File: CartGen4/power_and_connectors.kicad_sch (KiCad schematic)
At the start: 35 parts, among them U1 TPS65266-1RHBR

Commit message: Updated field information
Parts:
- A1: Notes (none) -> Edge connector and board outline of the cartridge
- C1, C10, C12, C13, C15, C16, C5, C6, C7, C8: Package ID (none) -> 0603
- C11, C2, C4, C9: Package ID (none) -> 0402
- C14, C17, C3: Notes (none) -> Used for loop compensation of SMPS; Package ID (none) -> 0402; Source (none) -> ANY
- C40: Critical (none) -> N; Notes (none) -> Coupling capacitor for isolating DC in audio signal; Package ID (none) -> 0603; Source (none) -> ANY
- L1, L2, L3: Notes (none) -> Filtering inductors for SMPS output; Package ID (none) -> 1008
- R1, R4, R8: Notes (none) -> Used for loop compensation of SMPS; Package ID (none) -> 0402
- R10, R2, R3, R5, R6, R9: Notes (none) -> Used for feedback attenuation of SMPS output; Package ID (none) -> 0402
- R12: Notes (none) -> Pullup resistor for PS_GOOD line; Package ID (none) -> 0402
- R19: Critical (none) -> N; Notes (none) -> Discharging resistor for audio coupling capacitor; Package ID (none) -> 0402; Source (none) -> ANY
- R7: Notes (none) -> Used to program the SMPS oscillator to 1MHz; Package ID (none) -> 0402

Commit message: Updated some component fields
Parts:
- C1, C5, C6, C7: Supplier suggestion (none) -> https://nl.mouser.com/ProductDetail/Samsung-Electro-Mechani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; Tolerance (none) -> 20%
- C10, C12, C13, C15, C16, C8: Supplier suggestion (none) -> https://nl.mouser.com/ProductDetail/Murata-Electronics/GRM1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; Tolerance (none) -> 20%; Voltage (none) -> 3V3
- C11, C4, C9: Supplier suggestion (none) -> https://nl.mouser.com/ProductDetail/Murata-Electronics/GRM1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; Tolerance (none) -> 5%
- C14, C17, C3: Supplier suggestion (none) -> https://nl.mouser.com/ProductDetail/Murata-Electronics/GRM1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; Tolerance (none) -> 5%; Voltage (none) -> 3V3
- C2: Supplier suggestion (none) -> https://nl.mouser.com/ProductDetail/Samsung-Electro-Mechani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; Tolerance (none) -> 20%; Voltage (none) -> 3V3
- C40: Supplier suggestion (none) -> https://nl.mouser.com/ProductDetail/Murata-Electronics/GCM1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
- L1, L2, L3: Supplier suggestion (none) -> https://nl.mouser.com/ProductDetail/Murata-Electronics/DFE2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
- R1: Supplier suggestion (none) -> https://nl.mouser.com/ProductDetail/ROHM-Semiconductor/ESR0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
- R10, R2, R3, R6: Supplier suggestion (none) -> https://nl.mouser.com/ProductDetail/YAGEO/RC0402DR-0710KL?q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
- R4, R5: Supplier suggestion (none) -> https://nl.mouser.com/ProductDetail/ROHM-Semiconductor/SFR0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

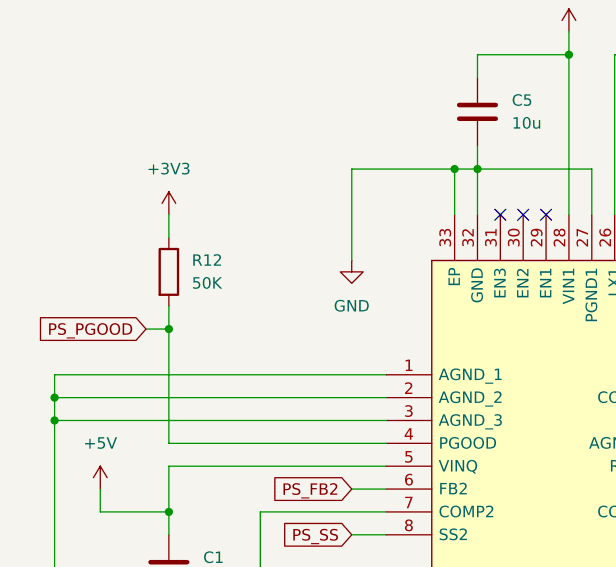
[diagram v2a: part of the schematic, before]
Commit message: Changed 50K size to 0603 due to unavailability
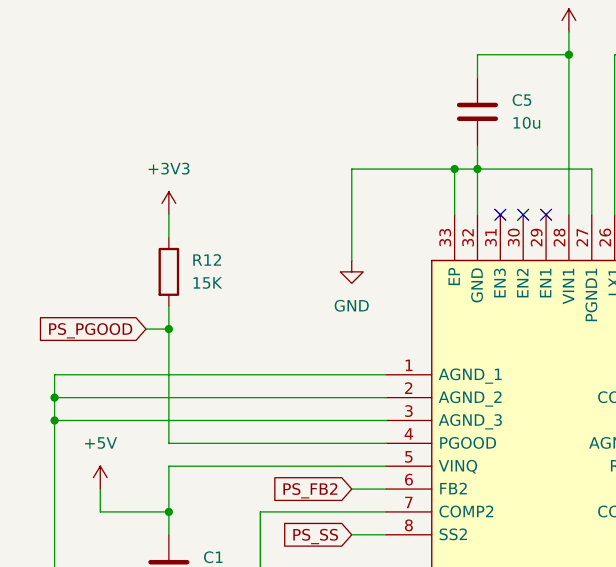
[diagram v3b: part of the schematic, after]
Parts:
- R12: value 50K -> 15K
- R7: footprint Resistor_SMD:R_0402_1005Metric_Pad0.72x0.64mm_HandSolder -> Resistor_SMD:R_0603_1608Metric_Pad0.98x0.95mm_HandSolder
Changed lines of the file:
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@@
       (effects (font (size 1.27 1.27)) (justify left))
     )
-    (property "Footprint" "Resistor_SMD:R_0402_1005Metric_Pad0.72x0.64mm_HandSolder" (id 2) (at 136.652 83.82 90)
+    (property "Footprint" "Resistor_SMD:R_0603_1608Metric_Pad0.98x0.95mm_HandSolder" (id 2) (at 136.652 83.82 90)
       (effects (font (size 1.27 1.27)) hide)
     )
@@
       (effects (font (size 1.27 1.27)) (justify left))
     )
-    (property "Value" "50K" (id 1) (at 45.72 57.1499 0)
-      (effects (font (size 1.27 1.27)) (justify left))
-    )
+    (property "Value" "15K" (id 1) (at 45.72 57.1499 0)
+      (effects (font (size 1.27 1.27)) (justify left))
+    )

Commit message: Revert "Changed 50K size to 0603 due to unavailability"
This reverts commit 7b462f06fc85ccc42ac1f7842e04da7b6c33922f.
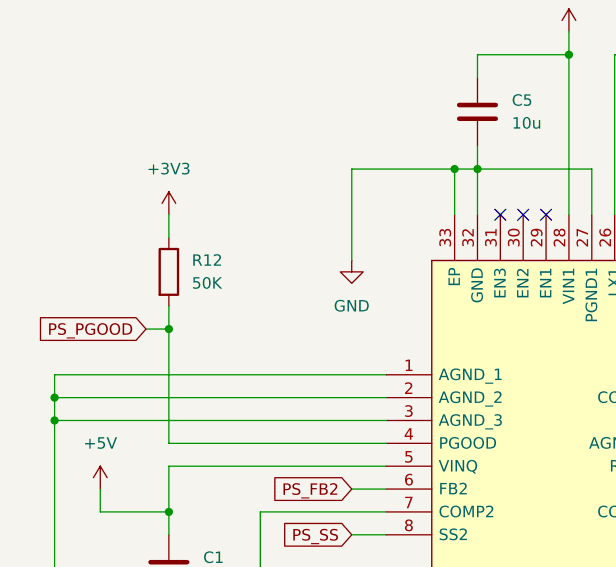
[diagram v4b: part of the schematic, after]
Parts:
- R12: value 15K -> 50K
- R7: footprint Resistor_SMD:R_0603_1608Metric_Pad0.98x0.95mm_HandSolder -> Resistor_SMD:R_0402_1005Metric_Pad0.72x0.64mm_HandSolder
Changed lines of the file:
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@@
       (effects (font (size 1.27 1.27)) (justify left))
     )
-    (property "Footprint" "Resistor_SMD:R_0603_1608Metric_Pad0.98x0.95mm_HandSolder" (id 2) (at 136.652 83.82 90)
+    (property "Footprint" "Resistor_SMD:R_0402_1005Metric_Pad0.72x0.64mm_HandSolder" (id 2) (at 136.652 83.82 90)
       (effects (font (size 1.27 1.27)) hide)
     )
@@
       (effects (font (size 1.27 1.27)) (justify left))
     )
-    (property "Value" "15K" (id 1) (at 45.72 57.1499 0)
-      (effects (font (size 1.27 1.27)) (justify left))
-    )
+    (property "Value" "50K" (id 1) (at 45.72 57.1499 0)
+      (effects (font (size 1.27 1.27)) (justify left))
+    )

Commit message: Added missing recommendations
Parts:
- R1, R4: Tolerance 10% -> 1%
- R12: value 50K -> 15K; Supplier suggestion (none) -> https://nl.mouser.com/ProductDetail/Kamaya/RMC1-16S-153JTH?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
- R19: Supplier suggestion (none) -> https://nl.mouser.com/ProductDetail/Walsin/WR04X224-JTL?qs=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; Tolerance (none) -> 10%
- R7: Supplier suggestion (none) -> https://nl.mouser.com/ProductDetail/Vishay-Dale/CRCW040250K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; Tolerance 10% -> 1%
- R8: Supplier suggestion (none) -> https://nl.mouser.com/ProductDetail/Vishay-Draloric/RCA0402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; Tolerance 10% -> 1%
- R9: Supplier suggestion (none) -> https://nl.mouser.com/ProductDetail/Panasonic/ERJ-2RKF2002X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
- U1: Supplier suggestion (none) -> https://nl.mouser.com/ProductDetail/Texas-Instruments/TPS65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
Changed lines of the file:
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@@
+      (effects (font (size 1.27 1.27)) hide)
+    )
+    (property "Supplier suggestion" "https://nl.mouser.com/ProductDetail/Walsin/WR04X224-JTL?qs=sGAEpiMZZMvdGkrng054t3TZKQOO49ydKJTYVsk%2Ff0A%3D" (id 11) (at 210.82 142.24 0)
+      (effects (font (size 1.27 1.27)) hide)
+    )
+    (property "Tolerance" "10%" (id 12) (at 210.82 142.24 0)
       (effects (font (size 1.27 1.27)) hide)
     )
@@
       (effects (font (size 1.27 1.27)) hide)
     )
-    (property "Tolerance" "10%" (id 4) (at 138.43 83.82 0)
+    (property "Tolerance" "1%" (id 4) (at 138.43 83.82 0)
       (effects (font (size 1.27 1.27)) hide)
     )
@@
     )
     (property "Package ID" "0402" (id 11) (at 138.43 83.82 0)
+      (effects (font (size 1.27 1.27)) hide)
+    )
+    (property "Supplier suggestion" "https://nl.mouser.com/ProductDetail/Vishay-Dale/CRCW040250K0FKED?qs=sGAEpiMZZMvdGkrng054t7ydTDqkWm6gHOJZVaVB4jo%3D" (id 12) (at 138.43 83.82 0)
       (effects (font (size 1.27 1.27)) hide)
     )
@@
       (effects (font (size 1.27 1.27)) (justify left))
     )
-    (property "Value" "50K" (id 1) (at 45.72 57.1499 0)
+    (property "Value" "15K" (id 1) (at 45.72 57.1499 0)
       (effects (font (size 1.27 1.27)) (justify left))
     )
@@
     )
     (property "Package ID" "0402" (id 11) (at 43.18 55.88 0)
+      (effects (font (size 1.27 1.27)) hide)
+    )
+    (property "Supplier suggestion" "https://nl.mouser.com/ProductDetail/Kamaya/RMC1-16S-153JTH?qs=sGAEpiMZZMvdGkrng054t%252BjmMOhbS7JJ11bN0iqZRdOn%2Fu9rqH1%2FEw%3D%3D" (id 12) (at 43.18 55.88 0)
       (effects (font (size 1.27 1.27)) hide)
     )
@@
       (effects (font (size 1.27 1.27)) hide)
     )
-    (property "Tolerance" "10%" (id 4) (at 147.32 69.85 0)
+    (property "Tolerance" "1%" (id 4) (at 147.32 69.85 0)
       (effects (font (size 1.27 1.27)) hide)
     )
@@
     )
     (property "Package ID" "0402" (id 11) (at 147.32 69.85 0)
+      (effects (font (size 1.27 1.27)) hide)
+    )
+    (property "Supplier suggestion" "https://nl.mouser.com/ProductDetail/Vishay-Draloric/RCA0402100KFKED?qs=sGAEpiMZZMvdGkrng054txHp3dxCF9fkIdgBS88QPBWM3ovdCYFY0A%3D%3D" (id 12) (at 147.32 69.85 0)
       (effects (font (size 1.27 1.27)) hide)
     )
@@
       (effects (font (size 1.27 1.27)) hide)
     )
+    (property "Supplier suggestion" "https://nl.mouser.com/ProductDetail/Panasonic/ERJ-2RKF2002X?qs=sGAEpiMZZMvdGkrng054t8ugkoYZivkgSHr6O6Hs91Q%3D" (id 12) (at 148.59 114.3 0)
+      (effects (font (size 1.27 1.27)) hide)
+    )
     (pin "1")
     (pin "2")
@@
       (effects (font (size 1.27 1.27)) hide)
     )
-    (property "Tolerance" "10%" (id 4) (at 121.92 82.55 0)
+    (property "Tolerance" "1%" (id 4) (at 121.92 82.55 0)
       (effects (font (size 1.27 1.27)) hide)
     )
@@
     )
     (property "Critical" "Y" (id 10) (at 67.31 67.31 0)
+      (effects (font (size 1.27 1.27)) hide)
+    )
+    (property "Supplier suggestion" "https://nl.mouser.com/ProductDetail/Texas-Instruments/TPS65266-1RHBR?qs=8N88piwwHEiYjq5W9uWjdA%3D%3D" (id 11) (at 67.31 67.31 0)
       (effects (font (size 1.27 1.27)) hide)
     )
@@
       (effects (font (size 1.27 1.27)) hide)
     )
-    (property "Tolerance" "10%" (id 4) (at 53.34 93.98 0)
-      (effects (font (size 1.27 1.27)) hide)
-    )
+    (property "Tolerance" "1%" (id 4) (at 53.34 93.98 0)
+      (effects (font (size 1.27 1.27)) hide)
+    )

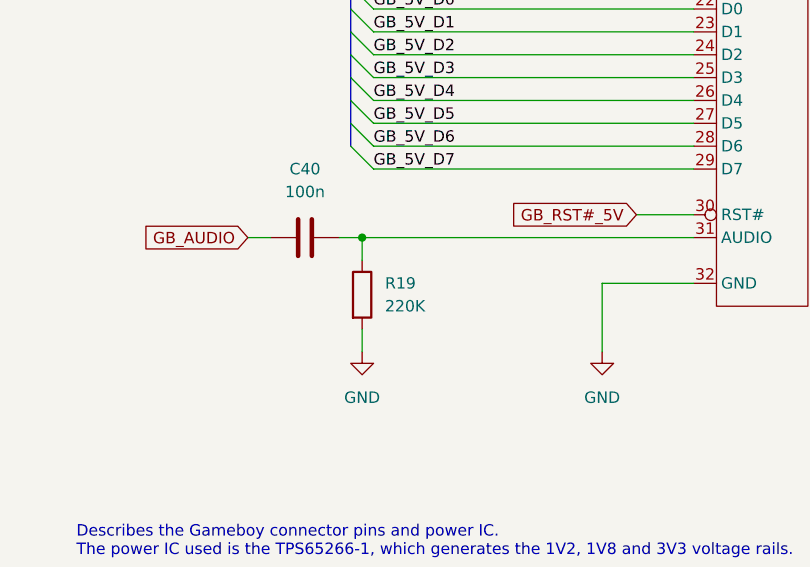
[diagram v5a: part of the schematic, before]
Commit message: Changed R19 to R13
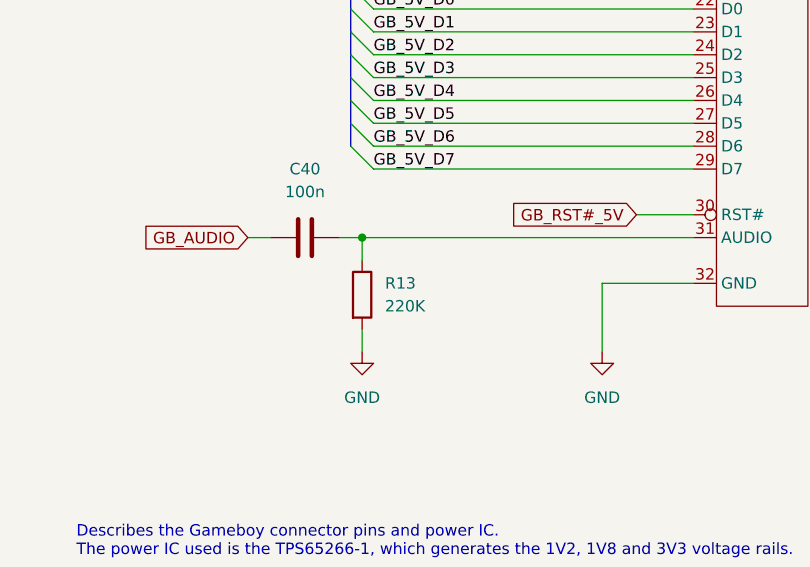
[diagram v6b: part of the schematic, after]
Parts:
- renumbered R19 to R13
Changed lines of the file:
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@@
   (symbol (lib_id "Device:R") (at 210.82 142.24 0) (unit 1)
     (in_bom yes) (on_board yes) (fields_autoplaced)
-    (property "Reference" "R19" (id 0) (at 213.36 140.9699 0)
+    (property "Reference" "R13" (id 0) (at 213.36 140.9699 0)
       (effects (font (size 1.27 1.27)) (justify left))
     )

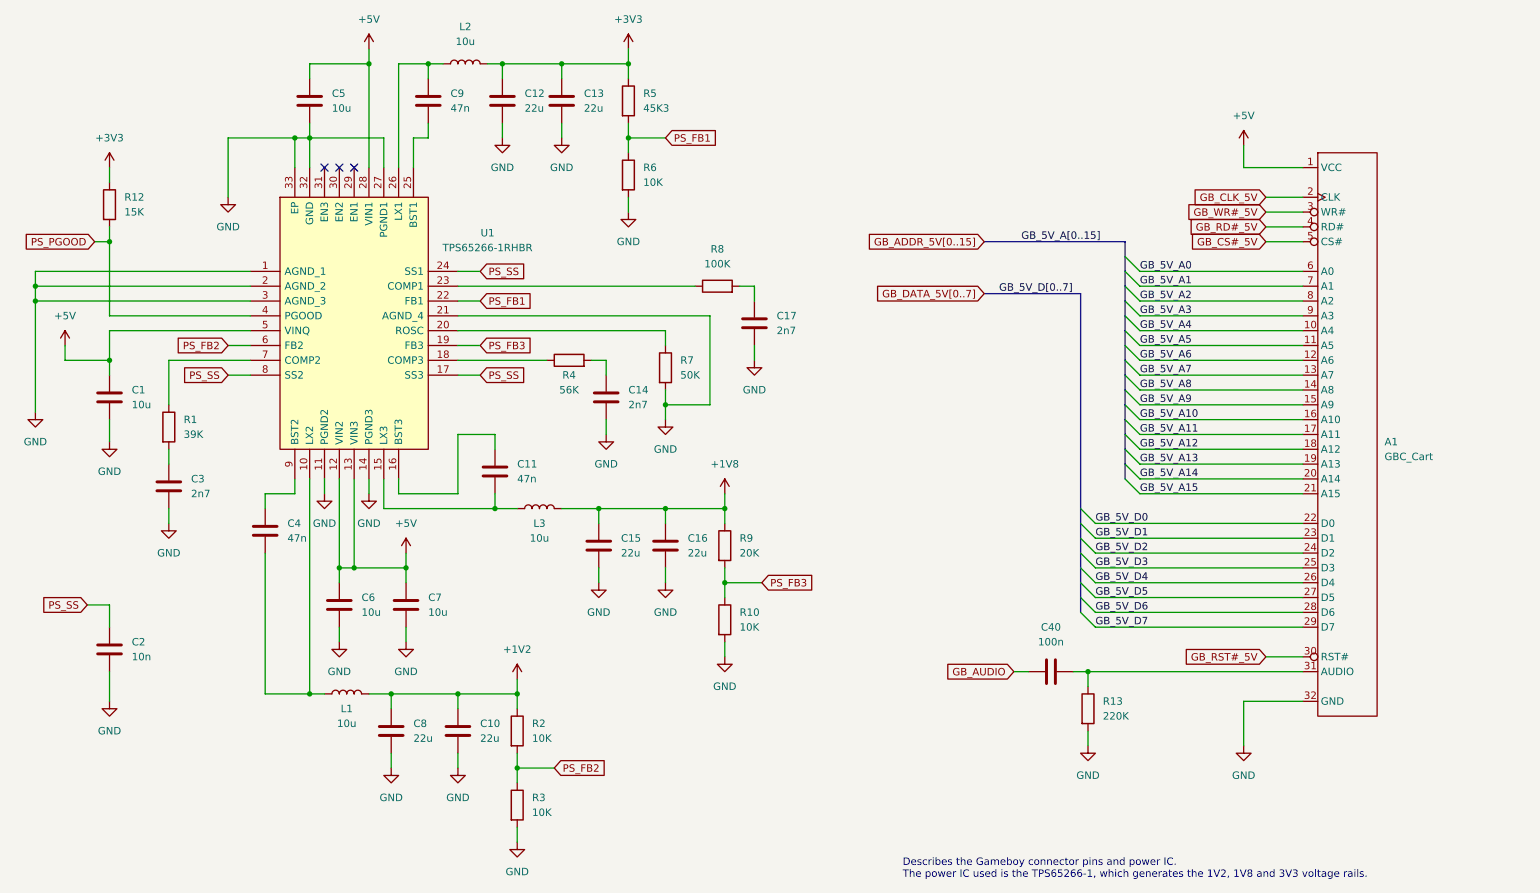
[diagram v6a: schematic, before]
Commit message: Reassigned RD geographically
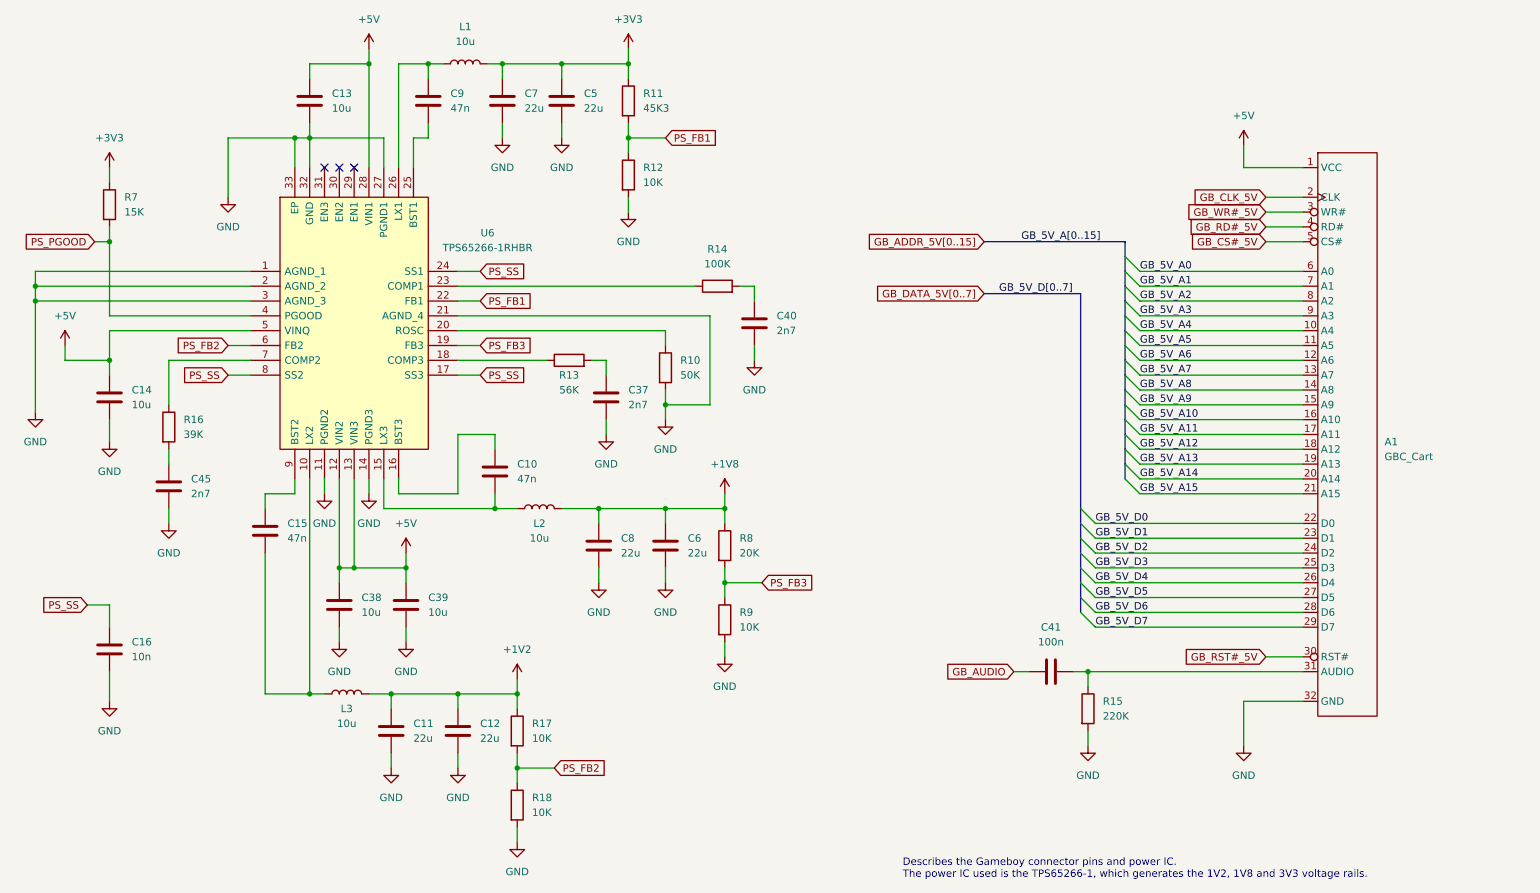
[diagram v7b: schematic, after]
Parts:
- renumbered C11 to C10, C8 to C11, C10 to C12, C5 to C13, C1 to C14, C4 to C15, C2 to C16, C14 to C37, C6 to C38, C7 to C39, C17 to C40, C40 to C41, C3 to C45, C13 to C5, C16 to C6, C12 to C7, C15 to C8, L2 to L1, L3 to L2, L1 to L3, R7 to R10, R5 to R11, R6 to R12, R4 to R13, R8 to R14, R13 to R15, R1 to R16, R2 to R17, R3 to R18, R12 to R7, R9 to R8, R10 to R9, U1 to U6

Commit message: Fixed silk screen placement Fixed RD misplacement Changed R16 supplier suggestion
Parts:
- R16: Supplier suggestion https://nl.mouser.com/ProductDetail/ROHM-Semiconductor/ESR0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 -> https://nl.mouser.com/ProductDetail/YAGEO/AC0402FR-0739KL?q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
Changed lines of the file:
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@@
       (effects (font (size 1.27 1.27)) hide)
     )
-    (property "Supplier suggestion" "https://nl.mouser.com/ProductDetail/ROHM-Semiconductor/ESR01MZPF3902?qs=sGAEpiMZZMvdGkrng054t2cqbZCzJY7NgClcB2OxpM9V0RG8k%252BPcGA%3D%3D" (id 12) (at 53.34 93.98 0)
+    (property "Supplier suggestion" "https://nl.mouser.com/ProductDetail/YAGEO/AC0402FR-0739KL?qs=sGAEpiMZZMvdGkrng054t1dXgLbs7QPXjrUf9Q5QEPg%3D" (id 12) (at 53.34 93.98 0)
       (effects (font (size 1.27 1.27)) hide)
     )
